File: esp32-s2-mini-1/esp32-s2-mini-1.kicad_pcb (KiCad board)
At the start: 2 copper layers, 33 x 58.4 mm, 17 parts, among them J1 Conn_01x04_Male, J2 USB_C_Receptacle_USB2.0, U1 ESP32-S2-MINI-1-N4_EXP, U2 LM1117-3.3

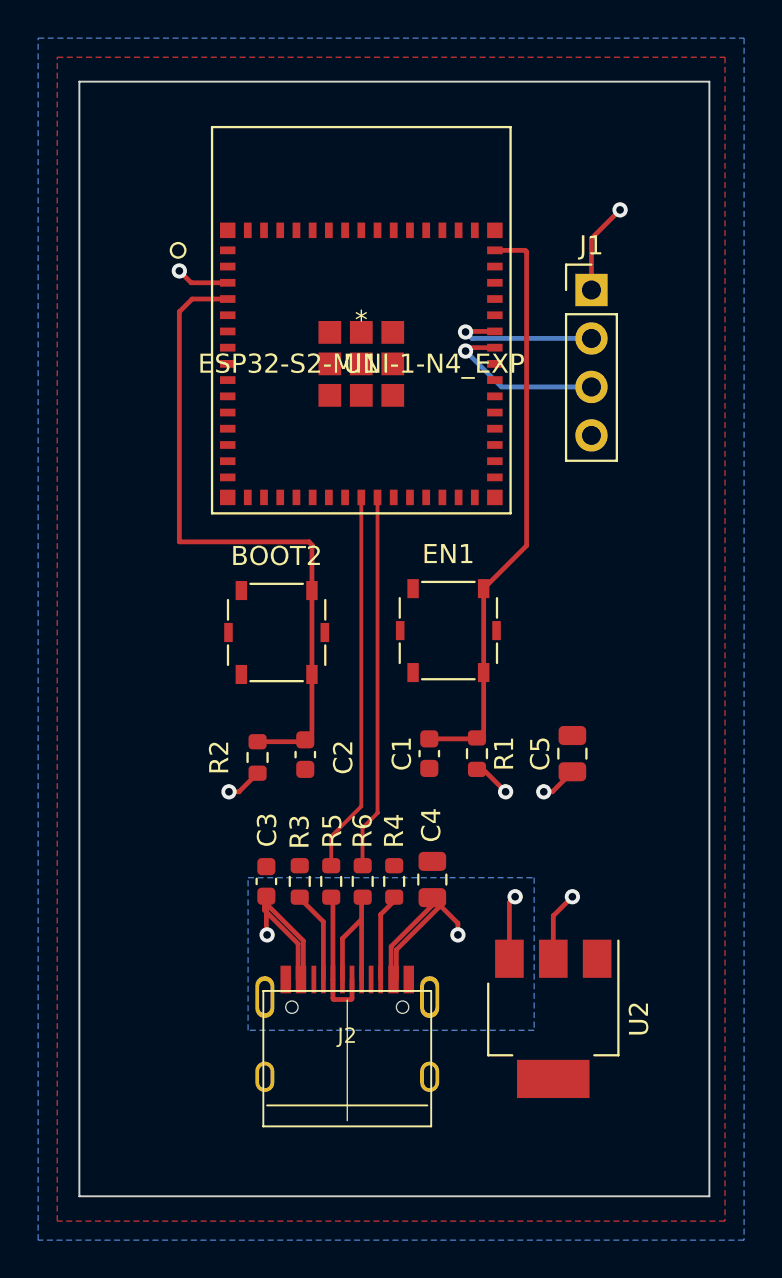
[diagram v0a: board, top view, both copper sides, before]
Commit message: The basic structure of the pcb is ready. Pins are unconnected, and extra components are missing still.
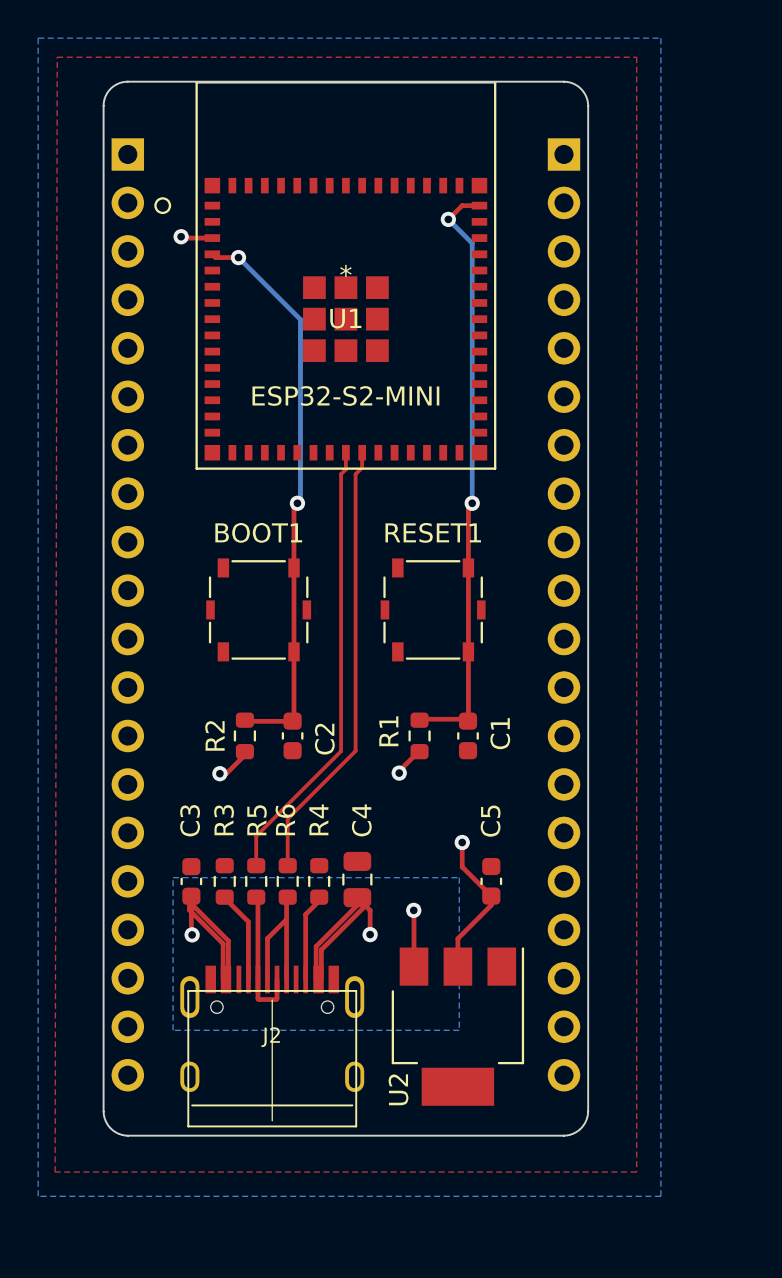
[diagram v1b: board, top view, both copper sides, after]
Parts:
- removed BOOT2, EN1: SW_Push, Button_Switch_SMD:SW_SPST_Panasonic_EVQPL_3PL_5PL_PT_A08
- added BOOT1: SW_Push, Button_Switch_SMD:SW_SPST_Panasonic_EVQPL_3PL_5PL_PT_A08, F.Cu at (146.6, 109.0)
- added J3: Conn_01x20_Male, Connector_PinHeader_2.54mm:PinHeader_1x20_P2.54mm_Vertical, B.Cu at (162.6, 85.1)
- added RESET1: SW_Push, Button_Switch_SMD:SW_SPST_Panasonic_EVQPL_3PL_5PL_PT_A08, F.Cu at (155.7, 109.0)
- C5: value 10uF -> 0.1uF; footprint Capacitor_SMD:C_0805_2012Metric -> Capacitor_SMD:C_0603_1608Metric
- J1: value Conn_01x04_Male -> Conn_01x20_Male; footprint Connector_PinHeader_2.54mm:PinHeader_1x04_P2.54mm_Vertical -> Connector_PinHeader_2.54mm:PinHeader_1x20_P2.54mm_Vertical; moved to B.Cu
- U1: value ESP32-S2-MINI-1-N4_EXP -> ESP32-S2-MINI
- moved J1 25.3 mm to (139.7, 85.1), turned to 180 degrees
- moved C5 7.93 mm to (158.8, 123.2)
- moved U2 5.02 mm to (157.0, 130.8)
- moved C3 3.93 mm to (143.0, 123.2)
- moved C4 3.93 mm to (151.7, 123.1)
- moved R3 3.93 mm to (144.8, 123.2)
- moved R4 3.93 mm to (149.7, 123.2)
- moved R5 3.93 mm to (146.4, 123.2)
- moved J2 3.93 mm to (147.3, 133.4)
- moved R6 3.93 mm to (148.1, 123.2)
- moved R1 3.15 mm to (155.0, 115.6)
- moved U1 2.48 mm to (151.1, 91.4)
- moved C1 2.23 mm to (157.5, 115.6)
- moved R2 1.31 mm to (145.8, 115.6)
- moved C2 1.18 mm to (148.3, 115.6)
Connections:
- J1 pad 1: +3V3 -> unconnected-(J1-Pad1)
- J1 pad 2: Net-(J1-Pad2) -> unconnected-(J1-Pad2)
- J1 pad 3: Net-(J1-Pad3) -> unconnected-(J1-Pad3)
- J1 pad 4: GND -> unconnected-(J1-Pad4)
- U1 pad 39: Net-(J1-Pad3) -> /TX
- U1 pad 40: Net-(J1-Pad2) -> /RX
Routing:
- net Net-(J1-Pad3): track 8.99 -> 0.00 mm, vias 1 -> 0
- net Net-(J1-Pad2): track 8.29 -> 0.00 mm, vias 1 -> 0
- net /BOOT: track 34.3 -> 29.7 mm, vias 0 -> 2
- net +3V3: track 17.1 -> 12.9 mm, vias 6 -> 4
- net USB_N: track 20.0 -> 23.6 mm
- net USB_P: track 19.6 -> 23.3 mm
- net +5V: track 27.5 -> 26.8 mm
- net /ENABLE: track 30.8 -> 31.3 mm, vias 0 -> 2
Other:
- board size 33 x 58.4 mm -> 25.4 x 55.2 mm

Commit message: Add power LED
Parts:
- added D1: LED, LED_SMD:LED_0603_1608Metric, F.Cu at (157.5, 123.2)
- added R7: 1K, Resistor_SMD:R_0603_1608Metric, F.Cu at (159.5, 123.2)
- moved C5 3.30 mm to (155.4, 123.2)
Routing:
- net Net-(D1-Pad1): track 0.00 -> 2.05 mm
- net +3V3: track 12.9 -> 11.4 mm
- net +5V: vias 3 -> 2
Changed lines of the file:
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@@
   (net 87 "unconnected-(U1-Pad5)")
   (net 88 "unconnected-(U1-Pad25)")
+  (net 89 "Net-(D1-Pad1)")
   (footprint "Package_TO_SOT_SMD:SOT-223" (layer "F.Cu")
     (at 157 130.81 -90)
@@
   )
   (footprint "Capacitor_SMD:C_0603_1608Metric" (layer "F.Cu")
-    (at 158.75 123.19 90)
+    (at 155.448 123.19 90)
     (descr "Capacitor SMD 0603 (1608 Metric), square (rectangular) end terminal, IPC_7351 nominal, (Body size source: IPC-SM-782 page 76, https://www.pcb-3d.com/wordpress/wp-content/uploads/ipc-sm-782a_amendment_1_and_2.pdf), generated with kicad-footprint-generator")
     (tags "capacitor")
@@
     (property "Sheetname" "")
     (attr smd)
-    (fp_text reference "C5" (at 3.175 0 90) (layer "F.SilkS")
+    (fp_text reference "C5" (at 3.048 0 90) (layer "F.SilkS")
       (effects (font (size 1 1) (thickness 0.15)))
     )
@@
       (net 3 "/BOOT") (pinfunction "2") (pintype "passive"))
     (model "${KICAD6_3DMODEL_DIR}/Button_Switch_SMD.3dshapes/SW_SPST_Panasonic_EVQPL_3PL_5PL_PT_A08.wrl"
+      (offset (xyz 0 0 0))
+      (scale (xyz 1 1 1))
+      (rotate (xyz 0 0 0))
+    )
+  )
+  (footprint "LED_SMD:LED_0603_1608Metric" (layer "F.Cu")
+    (at 157.48 123.19 -90)
+    (descr "LED SMD 0603 (1608 Metric), square (rectangular) end terminal, IPC_7351 nominal, (Body size source: http://www.tortai-tech.com/upload/download/2011102023233369053.pdf), generated with kicad-footprint-generator")
+    (tags "LED")
+    (property "Sheetfile" "esp32-s2-mini-1.kicad_sch")
+    (property "Sheetname" "")
+    (attr smd)
+    (fp_text reference "D1" (at -3.048 0 90) (layer "F.SilkS")
+      (effects (font (size 1 1) (thickness 0.15)))
+    )
+    (fp_text value "LED" (at 0 1.43 90) (layer "F.Fab")
+      (effects (font (size 1 1) (thickness 0.15)))
+    )
+    (fp_text user "${REFERENCE}" (at 0 0 90) (layer "F.Fab")
+      (effects (font (size 0.4 0.4) (thickness 0.06)))
+    )
+    (fp_line (start -1.485 -0.735) (end -1.485 0.735) (layer "F.SilkS") (width 0.12))
+    (fp_line (start -1.485 0.735) (end 0.8 0.735) (layer "F.SilkS") (width 0.12))
+    (fp_line (start 0.8 -0.735) (end -1.485 -0.735) (layer "F.SilkS") (width 0.12))
+    (fp_line (start -1.48 -0.73) (end 1.48 -0.73) (layer "F.CrtYd") (width 0.05))
+    (fp_line (start -1.48 0.73) (end -1.48 -0.73) (layer "F.CrtYd") (width 0.05))
+    (fp_line (start 1.48 -0.73) (end 1.48 0.73) (layer "F.CrtYd") (width 0.05))
+    (fp_line (start 1.48 0.73) (end -1.48 0.73) (layer "F.CrtYd") (width 0.05))
+    (fp_line (start -0.8 0.4) (end 0.8 0.4) (layer "F.Fab") (width 0.1))
+    (fp_line (start -0.8 -0.1) (end -0.8 0.4) (layer "F.Fab") (width 0.1))
+    (fp_line (start 0.8 -0.4) (end -0.5 -0.4) (layer "F.Fab") (width 0.1))
+    (fp_line (start -0.5 -0.4) (end -0.8 -0.1) (layer "F.Fab") (width 0.1))
+    (fp_line (start 0.8 0.4) (end 0.8 -0.4) (layer "F.Fab") (width 0.1))
+    (pad "1" smd roundrect (at -0.7875 0 270) (size 0.875 0.95) (layers "F.Cu" "F.Paste" "F.Mask") (roundrect_rratio 0.25)
+      (net 89 "Net-(D1-Pad1)") (pinfunction "K") (pintype "passive"))
+    (pad "2" smd roundrect (at 0.7875 0 270) (size 0.875 0.95) (layers "F.Cu" "F.Paste" "F.Mask") (roundrect_rratio 0.25)
+      (net 5 "+3V3") (pinfunction "A") (pintype "passive"))
+    (model "${KICAD6_3DMODEL_DIR}/LED_SMD.3dshapes/LED_0603_1608Metric.wrl"
       (offset (xyz 0 0 0))
       (scale (xyz 1 1 1))
@@
     )
   )
+  (footprint "Resistor_SMD:R_0603_1608Metric" (layer "F.Cu")
+    (at 159.512 123.19 90)
+    (descr "Resistor SMD 0603 (1608 Metric), square (rectangular) end terminal, IPC_7351 nominal, (Body size source: IPC-SM-782 page 72, https://www.pcb-3d.com/wordpress/wp-content/uploads/ipc-sm-782a_amendment_1_and_2.pdf), generated with kicad-footprint-generator")
+    (tags "resistor")
+    (property "Sheetfile" "esp32-s2-mini-1.kicad_sch")
+    (property "Sheetname" "")
+    (attr smd)
+    (fp_text reference "R7" (at 3.048 0 90) (layer "F.SilkS")
+      (effects (font (size 1 1) (thickness 0.15)))
+    )
+    (fp_text value "1K" (at 0 1.43 90) (layer "F.Fab")
+      (effects (font (size 1 1) (thickness 0.15)))
+    )
+    (fp_text user "${REFERENCE}" (at 0 0 90) (layer "F.Fab")
+      (effects (font (size 0.4 0.4) (thickness 0.06)))
+    )
+    (fp_line (start -0.237258 0.5225) (end 0.237258 0.5225) (layer "F.SilkS") (width 0.12))
+    (fp_line (start -0.237258 -0.5225) (end 0.237258 -0.5225) (layer "F.SilkS") (width 0.12))
+    (fp_line (start 1.48 -0.73) (end 1.48 0.73) (layer "F.CrtYd") (width 0.05))
+    (fp_line (start -1.48 0.73) (end -1.48 -0.73) (layer "F.CrtYd") (width 0.05))
+    (fp_line (start 1.48 0.73) (end -1.48 0.73) (layer "F.CrtYd") (width 0.05))
+    (fp_line (start -1.48 -0.73) (end 1.48 -0.73) (layer "F.CrtYd") (width 0.05))
+    (fp_line (start -0.8 0.4125) (end -0.8 -0.4125) (layer "F.Fab") (width 0.1))
+    (fp_line (start 0.8 -0.4125) (end 0.8 0.4125) (layer "F.Fab") (width 0.1))
+    (fp_line (start 0.8 0.4125) (end -0.8 0.4125) (layer "F.Fab") (width 0.1))
+    (fp_line (start -0.8 -0.4125) (end 0.8 -0.4125) (layer "F.Fab") (width 0.1))
+    (pad "1" smd roundrect (at -0.825 0 90) (size 0.8 0.95) (layers "F.Cu" "F.Paste" "F.Mask") (roundrect_rratio 0.25)
+      (net 1 "GND") (pintype "passive"))
+    (pad "2" smd roundrect (at 0.825 0 90) (size 0.8 0.95) (layers "F.Cu" "F.Paste" "F.Mask") (roundrect_rratio 0.25)
+      (net 89 "Net-(D1-Pad1)") (pintype "passive"))
+    (model "${KICAD6_3DMODEL_DIR}/Resistor_SMD.3dshapes/R_0603_1608Metric.wrl"
+      (offset (xyz 0 0 0))
+      (scale (xyz 1 1 1))
+      (rotate (xyz 0 0 0))
+    )
+  )
   (footprint "Connector_PinHeader_2.54mm:PinHeader_1x20_P2.54mm_Vertical" (layer "B.Cu")
     (at 139.7 85.095 180)
@@
   (segment (start 142.93 124.6975) (end 144.695 126.4625) (width 0.25) (layer "F.Cu") (net 4))
   (segment (start 152.4 124.7175) (end 151.73 124.0475) (width 0.25) (layer "F.Cu") (net 4))
-  (segment (start 154.686 124.714) (end 154.7 124.728) (width 0.25) (layer "F.Cu") (net 4))
   (segment (start 144.97 128.3375) (end 144.97 126.3125) (width 0.25) (layer "F.Cu") (net 4))
   (segment (start 142.93 124.2725) (end 142.93 124.6975) (width 0.25) (layer "F.Cu") (net 4))
   (segment (start 143.03 125.96) (end 143.07 126) (width 0.25) (layer "F.Cu") (net 4))
+  (segment (start 152.4 125.984) (end 154.076 127.66) (width 0.25) (layer "F.Cu") (net 4))
   (segment (start 152.4 125.984) (end 152.4 124.7175) (width 0.25) (layer "F.Cu") (net 4))
   (segment (start 143.03 123.9725) (end 143.03 125.96) (width 0.25) (layer "F.Cu") (net 4))
-  (segment (start 154.7 124.728) (end 154.7 127.66) (width 0.25) (layer "F.Cu") (net 4))
+  (segment (start 154.076 127.66) (end 154.7 127.66) (width 0.25) (layer "F.Cu") (net 4))
   (segment (start 149.845 126.7825) (end 152.325584 124.301916) (width 0.25) (layer "F.Cu") (net 4))
   (segment (start 144.97 126.3125) (end 142.93 124.2725) (width 0.25) (layer "F.Cu") (net 4))
-  (via (at 154.686 124.714) (size 0.8) (drill 0.4) (layers "F.Cu" "B.Cu") (net 4))
   (via (at 143.07 126) (size 0.8) (drill 0.4) (layers "F.Cu" "B.Cu") (net 4))
   (via (at 152.4 125.984) (size 0.8) (drill 0.4) (layers "F.Cu" "B.Cu") (net 4))
   (segment (start 144.130001 89.478515) (end 142.564515 89.478515) (width 0.25) (layer "F.Cu") (net 5))
+  (segment (start 157.4675 123.965) (end 157.48 123.9775) (width 0.25) (layer "F.Cu") (net 5))
+  (segment (start 155.448 123.965) (end 157.4675 123.965) (width 0.25) (layer "F.Cu") (net 5))
+  (segment (start 155.448 124.206) (end 155.448 123.965) (width 0.25) (layer "F.Cu") (net 5))
   (segment (start 144.861 117.55) (end 144.525 117.55) (width 0.25) (layer "F.Cu") (net 5))
-  (segment (start 157 126.195) (end 158.75 124.445) (width 0.25) (layer "F.Cu") (net 5))
+  (segment (start 156.718 125.476) (end 155.448 124.206) (width 0.25) (layer "F.Cu") (net 5))
   (segment (start 153.924 117.52) (end 153.924 117.411) (width 0.25) (layer "F.Cu") (net 5))
-  (segment (start 158.75 124.445) (end 158.75 123.965) (width 0.25) (layer "F.Cu") (net 5))
   (segment (start 153.924 117.411) (end 154.99 116.345) (width 0.25) (layer "F.Cu") (net 5))
-  (segment (start 157.226 121.158) (end 157.226 122.441) (width 0.25) (layer "F.Cu") (net 5))
-  (segment (start 157.226 122.441) (end 158.75 123.965) (width 0.25) (layer "F.Cu") (net 5))
+  (segment (start 157 125.758) (end 157 127.66) (width 0.25) (layer "F.Cu") (net 5))
   (segment (start 142.564515 89.478515) (end 142.494 89.408) (width 0.25) (layer "F.Cu") (net 5))
-  (segment (start 157 127.66) (end 157 126.195) (width 0.25) (layer "F.Cu") (net 5))
+  (segment (start 156.718 125.476) (end 157 125.758) (width 0.25) (layer "F.Cu") (net 5))
   (segment (start 145.836 116.575) (end 144.861 117.55) (width 0.25) (layer "F.Cu") (net 5))
-  (via (at 157.226 121.158) (size 0.8) (drill 0.4) (layers "F.Cu" "B.Cu") (net 5))
   (via (at 142.494 89.408) (size 0.8) (drill 0.4) (layers "F.Cu" "B.Cu") (net 5))
+  (via (at 156.718 125.476) (size 0.8) (drill 0.4) (layers "F.Cu" "B.Cu") (net 5))
   (via (at 153.924 117.52) (size 0.8) (drill 0.4) (layers "F.Cu" "B.Cu") (net 5))
   (via (at 144.525 117.55) (size 0.8) (drill 0.4) (layers "F.Cu" "B.Cu") (net 5))
@@
   (segment (start 148.08 122.3725) (end 148.08 119.92) (width 0.2) (layer "F.Cu") (net 13))
   (segment (start 148.08 119.92) (end 151.638 116.362) (width 0.2) (layer "F.Cu") (net 13))
+  (segment (start 159.4745 122.4025) (end 159.512 122.365) (width 0.25) (layer "F.Cu") (net 89))
+  (segment (start 157.48 122.4025) (end 159.4745 122.4025) (width 0.25) (layer "F.Cu") (net 89))
   (zone (net 1) (net_name "GND") (layer "F.Cu") (hatch edge 0.508)
     (connect_pads (clearance 0.25))
@@
     (polygon
       (pts
-        (xy 157.07 131)
-        (xy 142.07 131)
+        (xy 153.416 125.984)
+        (xy 155.936098 126.00753)
+        (xy 155.956 129.54)
+        (xy 142.07 129.54)
         (xy 142.07 123)
-        (xy 157.07 123)
+        (xy 153.416 122.936)
       )
     )
